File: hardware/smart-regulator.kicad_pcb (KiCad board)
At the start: 2 copper layers, 66 x 56 mm, 73 parts, among them J2 Conn_02x20_Odd_Even, P1 USB_A_2, SW1 SW_PUSH, SW2 SW_PUSH, SW3 SW_PUSH, U1 ESP-WROOM-32, U10 Power-Monitor-INA219, U11 DAC, U12 ZLDO1117G33TA, U14 SI7006-A20, U15 TSL45315CL, U2 housing-mounts, U3 MIC29302, U4 MIC29302, U5 MIC29302, U6 MIC29302, U7 ACS712ELCTR-05B-T_NRND, U8 Power-Monitor-INA219, U9 Power-Monitor-INA219

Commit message: silkscreen
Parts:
- added LOGO: , open-automation:LOGO, B.Cu at (160.1, 102.0)
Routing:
- net /EN: track 18.8 -> 20.0 mm
- net 3V3: track 245.9 -> 245.2 mm, vias 37 -> 33

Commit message: series ender
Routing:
- net 3V3: track 245.2 -> 247.5 mm
- net GND: track 130.4 -> 129.2 mm, vias 43 -> 41
- net /PACK3: track 57.3 -> 56.6 mm
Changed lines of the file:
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@@
     (thickness 1.6)
     (drawings 14)
-    (tracks 1312)
+    (tracks 1307)
     (zones 0)
     (modules 74)
@@
   )
   (setup
-    (last_trace_width 0.4)
+    (last_trace_width 0.15)
     (user_trace_width 0.15)
     (user_trace_width 0.25)
@@
   (segment (start 145.8 118) (end 145.8 118.2) (width 0.15) (layer F.Cu) (net 1))
   (segment (start 145.8 118) (end 145.8 118.4) (width 0.15) (layer F.Cu) (net 1))
-  (via (at 143.176936 122.116699) (size 0.6) (drill 0.4) (layers F.Cu B.Cu) (net 1))
   (segment (start 143.176936 121.023064) (end 143.176936 122.116699) (width 0.15) (layer F.Cu) (net 1))
   (segment (start 145.8 118.4) (end 143.176936 121.023064) (width 0.15) (layer F.Cu) (net 1))
@@
   (segment (start 155 85.58) (end 154.56 85.14) (width 0.15) (layer F.Cu) (net 1))
   (segment (start 155 89) (end 155 85.58) (width 0.15) (layer F.Cu) (net 1))
-  (via (at 146.5 124.2) (size 0.6) (drill 0.4) (layers F.Cu B.Cu) (net 1))
-  (segment (start 146.892 123.408) (end 146.892 123.808) (width 0.15) (layer B.Cu) (net 1))
-  (segment (start 146.892 123.808) (end 146.5 124.2) (width 0.15) (layer B.Cu) (net 1))
-  (via (at 145.4 122.2) (size 0.6) (drill 0.4) (layers F.Cu B.Cu) (net 1))
-  (segment (start 145.298 122.098) (end 145.4 122.2) (width 0.15) (layer B.Cu) (net 1))
-  (segment (start 144.192 122.098) (end 145.298 122.098) (width 0.15) (layer B.Cu) (net 1))
-  (segment (start 146.5 123.3) (end 146.5 124.2) (width 0.15) (layer F.Cu) (net 1))
-  (segment (start 145.4 122.2) (end 146.5 123.3) (width 0.15) (layer F.Cu) (net 1))
   (via (at 151.1 105.6) (size 0.6) (drill 0.4) (layers F.Cu B.Cu) (net 1))
   (segment (start 151.164 105.536) (end 151.1 105.6) (width 0.15) (layer B.Cu) (net 1))
@@
   (segment (start 168.597343 132.027657) (end 168.694856 132.027657) (width 0.2) (layer F.Cu) (net 1))
   (segment (start 168.694856 132.027657) (end 168.994855 132.327656) (width 0.2) (layer F.Cu) (net 1))
+  (segment (start 145.122 122.098) (end 144.192 122.098) (width 0.15) (layer B.Cu) (net 1))
+  (segment (start 145.697012 122.673012) (end 145.122 122.098) (width 0.15) (layer B.Cu) (net 1))
+  (segment (start 145.962 123.408) (end 145.697012 123.143012) (width 0.15) (layer B.Cu) (net 1))
+  (segment (start 146.892 123.408) (end 145.962 123.408) (width 0.15) (layer B.Cu) (net 1))
+  (segment (start 145.697012 123.143012) (end 145.697012 122.673012) (width 0.15) (layer B.Cu) (net 1))
+  (via (at 143.176936 122.116699) (size 0.6) (drill 0.4) (layers F.Cu B.Cu) (net 1))
   (segment (start 134.225 129.125) (end 134.45 128.9) (width 0.25) (layer F.Cu) (net 2))
   (segment (start 132.75 129.125) (end 134.225 129.125) (width 0.25) (layer F.Cu) (net 2))
@@
   (segment (start 150.6 124.5) (end 148.907999 122.807999) (width 0.4) (layer B.Cu) (net 4))
   (via (at 144.2 124.9) (size 0.6) (drill 0.4) (layers F.Cu B.Cu) (net 4))
-  (segment (start 145.6 124.6) (end 145.6 124.130702) (width 0.15) (layer B.Cu) (net 4))
-  (segment (start 145.836999 122.883001) (end 145.962 122.758) (width 0.15) (layer B.Cu) (net 4))
-  (segment (start 145.6 124.130702) (end 145.836999 123.893703) (width 0.15) (layer B.Cu) (net 4))
   (via (at 145.6 124.6) (size 0.6) (drill 0.4) (layers F.Cu B.Cu) (net 4))
   (via (at 142.7 125.2) (size 0.6) (drill 0.4) (layers F.Cu B.Cu) (net 4))
-  (segment (start 145.836999 123.893703) (end 145.836999 122.883001) (width 0.15) (layer B.Cu) (net 4))
-  (segment (start 145.962 122.758) (end 146.892 122.758) (width 0.15) (layer B.Cu) (net 4))
   (segment (start 144.5 124.6) (end 144.2 124.9) (width 0.4) (layer F.Cu) (net 4))
   (segment (start 145.6 124.6) (end 144.5 124.6) (width 0.4) (layer F.Cu) (net 4))
@@
   (segment (start 130.725 95.575) (end 130.75 95.55) (width 0.4) (layer F.Cu) (net 4))
   (segment (start 130.725 97.075) (end 130.725 95.575) (width 0.4) (layer F.Cu) (net 4))
+  (segment (start 148.825091 124.241136) (end 145.958864 124.241136) (width 0.4) (layer B.Cu) (net 4))
+  (segment (start 145.958864 124.241136) (end 145.6 124.6) (width 0.4) (layer B.Cu) (net 4))
+  (segment (start 150.6 124.5) (end 149.083955 124.5) (width 0.4) (layer B.Cu) (net 4))
+  (segment (start 149.083955 124.5) (end 148.825091 124.241136) (width 0.4) (layer B.Cu) (net 4))
   (segment (start 144.122 108.085) (end 145.087 108.085) (width 0.25) (layer B.Cu) (net 23))
   (segment (start 132.225 89.175) (end 132.275 89.225) (width 1) (layer F.Cu) (net 23))
@@
   (segment (start 166.4 118.2) (end 163.4 118.2) (width 1) (layer F.Cu) (net 68))
   (segment (start 163.4 118.2) (end 160.3 121.3) (width 1) (layer F.Cu) (net 68))
-  (via (at 148.8 124.9) (size 1.5) (drill 1) (layers F.Cu B.Cu) (net 68))
-  (segment (start 148.5975 124.9) (end 146.7515 126.746) (width 1) (layer B.Cu) (net 68))
-  (segment (start 148.8 124.9) (end 148.5975 124.9) (width 1) (layer B.Cu) (net 68))
   (via (at 153.3 123.06621) (size 1.5) (drill 1) (layers F.Cu B.Cu) (net 68))
   (segment (start 160.3 121.3) (end 155.06621 121.3) (width 1) (layer B.Cu) (net 68))
@@
   (segment (start 137.10001 134.149264) (end 137.675736 134.72499) (width 0.25) (layer B.Cu) (net 68))
   (segment (start 137.10001 132.89999) (end 137.10001 134.149264) (width 0.25) (layer B.Cu) (net 68))
-  (segment (start 152.23934 123.06621) (end 153.3 123.06621) (width 1) (layer F.Cu) (net 68))
-  (segment (start 149.57313 123.06621) (end 152.23934 123.06621) (width 1) (layer F.Cu) (net 68))
-  (segment (start 148.8 123.83934) (end 149.57313 123.06621) (width 1) (layer F.Cu) (net 68))
-  (segment (start 148.8 124.9) (end 148.8 123.83934) (width 1) (layer F.Cu) (net 68))
   (segment (start 142.344072 123.198928) (end 142.83607 123.198928) (width 0.25) (layer B.Cu) (net 68))
   (segment (start 143.276998 122.758) (end 144.192 122.758) (width 0.25) (layer B.Cu) (net 68))
@@
   (segment (start 146.7515 128.971778) (end 146.804712 129.02499) (width 0.25) (layer B.Cu) (net 68))
   (segment (start 149.897647 129.324989) (end 150.197646 129.02499) (width 0.25) (layer B.Cu) (net 68))
-  (segment (start 144.974999 124.969499) (end 145.91829 125.91279) (width 0.25) (layer B.Cu) (net 68))
-  (segment (start 144.192 122.758) (end 144.259002 122.825002) (width 0.25) (layer B.Cu) (net 68))
+  (segment (start 150.598017 123.06621) (end 149.023089 124.641138) (width 1) (layer F.Cu) (net 68))
+  (segment (start 149.023089 124.641138) (end 148.27309 125.391137) (width 1) (layer F.Cu) (net 68))
+  (segment (start 153.3 123.06621) (end 150.598017 123.06621) (width 1) (layer F.Cu) (net 68))
+  (segment (start 148.106363 125.391137) (end 148.27309 125.391137) (width 1) (layer B.Cu) (net 68))
+  (segment (start 146.7515 126.746) (end 148.106363 125.391137) (width 1) (layer B.Cu) (net 68))
+  (via (at 148.27309 125.391137) (size 1.5) (drill 1) (layers F.Cu B.Cu) (net 68))
+  (segment (start 144.316999 122.882999) (end 145.232001 122.882999) (width 0.25) (layer B.Cu) (net 68))
+  (segment (start 144.192 122.758) (end 144.316999 122.882999) (width 0.25) (layer B.Cu) (net 68))
   (segment (start 144.974999 124.190003) (end 144.974999 124.969499) (width 0.25) (layer B.Cu) (net 68))
+  (segment (start 144.974999 124.969499) (end 145.91829 125.91279) (width 0.25) (layer B.Cu) (net 68))
+  (segment (start 145.297001 123.868001) (end 144.974999 124.190003) (width 0.25) (layer B.Cu) (net 68))
+  (segment (start 145.297001 122.947999) (end 145.297001 123.868001) (width 0.25) (layer B.Cu) (net 68))
   (segment (start 145.91829 125.91279) (end 146.7515 126.746) (width 0.25) (layer B.Cu) (net 68))
-  (segment (start 145.299999 122.835999) (end 145.299999 123.865003) (width 0.25) (layer B.Cu) (net 68))
-  (segment (start 145.289002 122.825002) (end 145.299999 122.835999) (width 0.25) (layer B.Cu) (net 68))
-  (segment (start 144.259002 122.825002) (end 145.289002 122.825002) (width 0.25) (layer B.Cu) (net 68))
-  (segment (start 145.299999 123.865003) (end 144.974999 124.190003) (width 0.25) (layer B.Cu) (net 68))
+  (segment (start 145.232001 122.882999) (end 145.297001 122.947999) (width 0.25) (layer B.Cu) (net 68))
   (segment (start 154.4495 95.185) (end 157.485 95.185) (width 1) (layer B.Cu) (net 69))
   (segment (start 163.120001 96.710001) (end 166.37 99.96) (width 1) (layer B.Cu) (net 69))

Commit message: rewire
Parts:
- removed LOGO: , open-automation:LOGO
- moved C4 11.2 mm to (133.2, 99.4), turned to 180 degrees
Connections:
- C10 pad 1: GND -> 3V3
- C4 pad 1: /Power/REG_POWER -> MAIN_CURRENT_SENSE
- C8 pad 1: GND -> 3V3
- C9 pad 1: GND -> 3V3
- U1 pad 7: Net-(U1-Pad7) -> /REG2_EN
- U1 pad 9: /REG2_EN -> MAIN_CURRENT_SENSE
- U7 pad 11: /Power/REG_POWER -> MAIN_CURRENT_SENSE
- U8 pad 7: 3V3 -> /SDA
- U9 pad 7: 3V3 -> GND
- U9 pad 8: GND -> 3V3
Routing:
- net MAIN_CURRENT_SENSE: track 0.00 -> 39.2 mm, vias 0 -> 10
- net 3V3: track 247.5 -> 259.1 mm, vias 33 -> 34
- net GND: track 129.2 -> 139.4 mm
- net /Power/REG_POWER: track 113.4 -> 112.0 mm
- net /REG2_EN: track 19.4 -> 18.0 mm
- net /SDA: track 104.5 -> 105.6 mm
- net /Power/OUT2: track 41.6 -> 42.3 mm
- net /REG1_EN: track 45.8 -> 46.4 mm

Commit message: corrected error on schem/layout
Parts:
- added R26: R_10k, Resistor_SMD:R_0603_1608Metric_Pad1.05x0.95mm_HandSolder, F.Cu at (133.3, 101.2)
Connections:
- C10 pad 1: 3V3 -> GND
- C10 pad 2: Net-(C10-Pad2) -> 3V3
- C8 pad 1: 3V3 -> GND
- C8 pad 2: Net-(C8-Pad2) -> 3V3
- C9 pad 1: 3V3 -> GND
- C9 pad 2: Net-(C9-Pad2) -> 3V3
- U10 pad 4: Net-(C10-Pad2) -> 3V3
- U8 pad 4: Net-(C8-Pad2) -> 3V3
- U9 pad 4: Net-(C9-Pad2) -> 3V3
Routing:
- net GND: track 139.4 -> 144.9 mm, vias 41 -> 42
- net Net-(C8-Pad2): track 4.88 -> 0.00 mm
- net 3V3: track 259.1 -> 263.0 mm, vias 34 -> 32
- net Net-(C10-Pad2): track 2.54 -> 0.00 mm
- net Net-(C9-Pad2): track 2.37 -> 0.00 mm
- net MAIN_CURRENT_SENSE: track 39.2 -> 41.0 mm
- net /PACK3: track 56.6 -> 57.6 mm

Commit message: update before try #3
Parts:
- D4, D5, D6: footprint open-automation:SOD128 -> Diode_SMD:D_SMC
- U12: moved to B.Cu
- moved R14 4.22 mm to (132.9, 134.1)
- moved R13 4.19 mm to (133.0, 132.6)
- moved D4 3.99 mm to (141.2, 131.2)
- moved D5 1.11 mm to (153.2, 116.8)
- moved C6 0.76 mm to (140.6, 123.0)
- moved D6 0.70 mm to (153.7, 100.3)
- moved C10 0.54 mm to (140.6, 121.5)
- moved U12 0.17 mm to (170.4, 126.8)
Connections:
- U12 pad 1: Net-(D7-Pad1) -> GND
- U12 pad 3: GND -> Net-(D7-Pad1)
- U12 pad 4: (no net) -> 3V3
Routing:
- net GND: track 144.9 -> 157.1 mm, vias 42 -> 48
- net 3V3: track 263.0 -> 270.6 mm, vias 32 -> 31
- net /RXD: track 77.1 -> 83.1 mm
- net /Power/OUT3: track 74.4 -> 78.7 mm, vias 5 -> 3
- net /USB_EN: track 44.7 -> 48.1 mm
- net /V_MAIN: track 40.9 -> 43.8 mm
- net /PACK3: track 57.6 -> 60.0 mm
- net /Power/REG3_PRE: track 18.4 -> 20.4 mm
- net /Power/REG1_PRE: track 17.9 -> 19.4 mm
- net /Power/OUT2: track 42.3 -> 43.7 mm
- net /SDA: track 105.6 -> 106.8 mm
- net /PACK1: track 35.0 -> 36.0 mm
- net /Power/REG2_PRE: track 18.0 -> 17.3 mm
- net /SCL: track 105.3 -> 105.9 mm
- net Net-(D7-Pad1): track 16.2 -> 16.4 mm, vias 1 -> 2
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
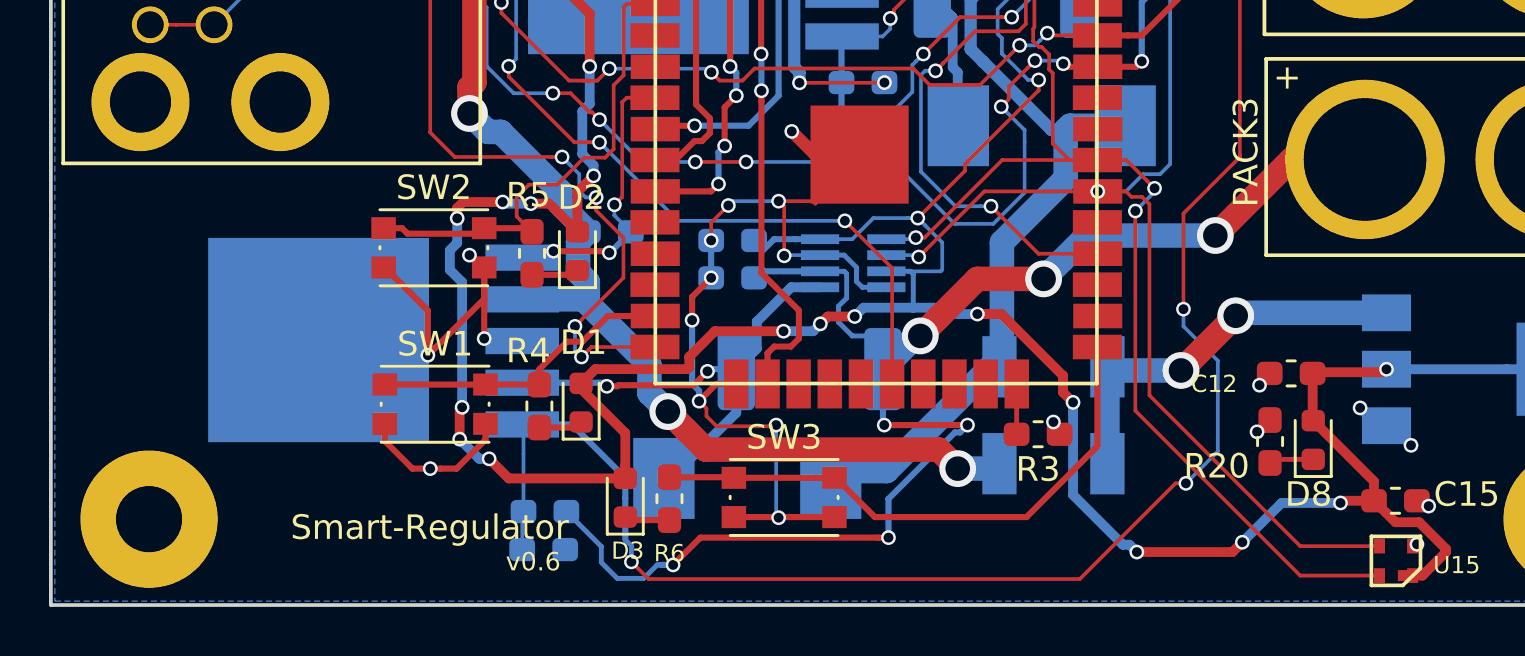
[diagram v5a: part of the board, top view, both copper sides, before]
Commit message: fixed footprint missmatch on diodes/final touchups
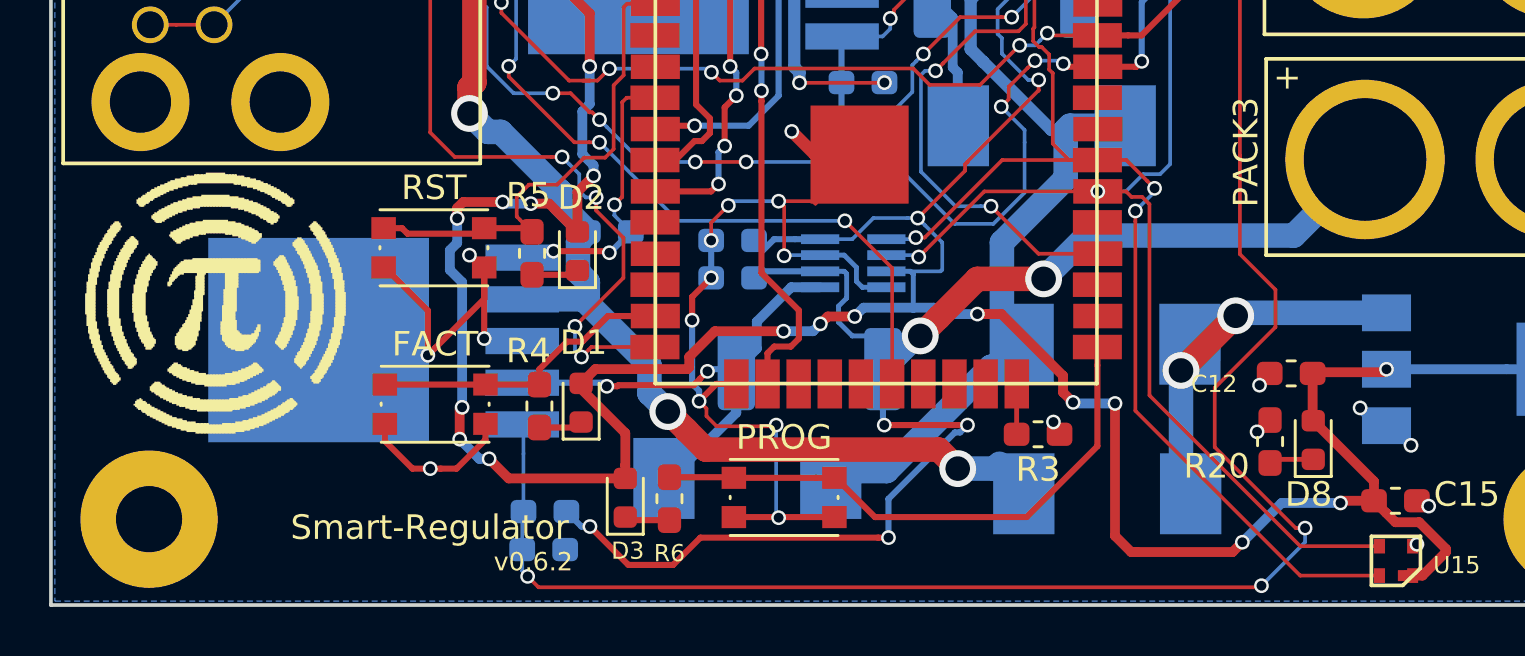
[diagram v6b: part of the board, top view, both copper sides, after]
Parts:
- added LOGO: , open-automation:pyfi_symbol, F.Cu at (114.2, 118.7)
- D7, D9: footprint open-automation:SOD128 -> Diode_SMD:D_SMC
- moved D9 1.23 mm to (155.9, 131.8)
- moved D7 0.92 mm to (155.9, 125.7)
- renumbered SW1 to FACT, SW3 to PROG, SW2 to RST
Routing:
- net /Power/OUT3: track 78.7 -> 83.1 mm
- net 3V3: track 270.6 -> 271.5 mm
- net /PACK3: track 60.0 -> 59.1 mm, vias 7 -> 6
- net Net-(D7-Pad1): track 16.4 -> 17.0 mm
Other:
- board text added: "v0.6.2"
- board text removed: "v0.6"
